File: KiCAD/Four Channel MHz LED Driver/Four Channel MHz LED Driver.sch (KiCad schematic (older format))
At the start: 89 parts, among them J1 Barrel_Jack_Switch, J10 Conn_01x08_Female, J2 Conn_01x02_Female, J3 8P8C_Shielded_x4, J4 Conn_01x05_Female, J5 Conn_01x24_Female, J6 Conn_01x03_Male, J7 Conn_01x24_Female, J8 Conn_01x03_Female, J9 Conn_01x03_Female, M1 Fan_4pin, Q2 SUM70060E, SW1 SW_SPDT, SW2 Pushbutton_with_LED_-_ELUMOAT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, SW3 Pushbutton_with_LED_-_ELUMOAT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, SW4 Pushbutton_with_LED_-_ELUMOAT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, SW5 Pushbutton_with_LED_-_ELUMOAT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, U1 12V boost, U10 LT6200CS8-10, U14 Teensy3.6, U16 SN74LV4T125PWR, U2 ASSR-1218, U3 DPBW06F-05, U4 BDJ0GA5WEFJ-E2, U5 ADP7182AUJZ-1.8-R7, U6 TMUX1204DGSR, U7 ASSR-1218, U8 ASSR-1218, U9 ASSR-1218

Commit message: Organized schematic
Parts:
- SW2, SW3, SW4, SW5: value Pushbutton_with_LED_-_ELUMOATHQ3C12 -> Pushbutton_with_LED
- renumbered C14 to C10, C15 to C11, C17 to C12, C34 to C13, C16 to C14, C9 to C15, C37 to C16, C19 to C17, C20 to C18, C12 to C19, C13 to C20, C23 to C21, C5 to C4, C6 to C5, C7 to C6, C10 to C7, C4 to C9, D4 to D3, D11 to D4, R5 to R1, R1 to R2, R2 to R5
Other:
- note added: "3.3V clamp for external analog\nMax voltage: +6V/-3V"
- note added: "4-pin 92mm fan"
- note added: "4x momentary pushbuttons with indicator LEDs"
- note added: "Constant Current LED Driver with Compensation\n\n"
- note added: "External analog input with 3.3V zener clamp"
- note added: "External thermistor and 3x 5V/16mA digital outputs\n"
- note added: "Inputs and Outputs\n"
- note added: "LED Solid-State Relay Mux\n\n"
- note added: "LED bypass capacitor array"
- note added: "Op-amp linear reagulator split supply: \n12V/-5V to clean 10V/-1.8V"
- note added: "Teensy 3.6 180 MHz Microcontroller"
- note added: "Thermal Management\n"
- note added: "Voltage Rails: 12V, 10V, 5V, -0.25V, -1.8V, -5V\n\n"
- note removed: "4-channel op-amp constant current LED driver"
- note removed: "External analog inputs with 5.6V zener clamp"
- note removed: "External thermistor and 3x 5V/16mA digital outputs\nOpen jumper for DAC output instead"
- note removed: "LDO: 12V to clean 5V for analog circuits"
- note removed: "LED bypass capacitors and connectors\nFor high current supplies use an in-line\ncapacitor with the power supply such as:\nUnited Chemi-Con E32D500HPN104MDA5M"
- note removed: "Op-amp split supply: 12V/-5V to clean 10V/-1.8V"
- moved on the sheet: BZ1, C1, C10, C11, C12, C13, C14, C17, C18, C19, C2, C20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

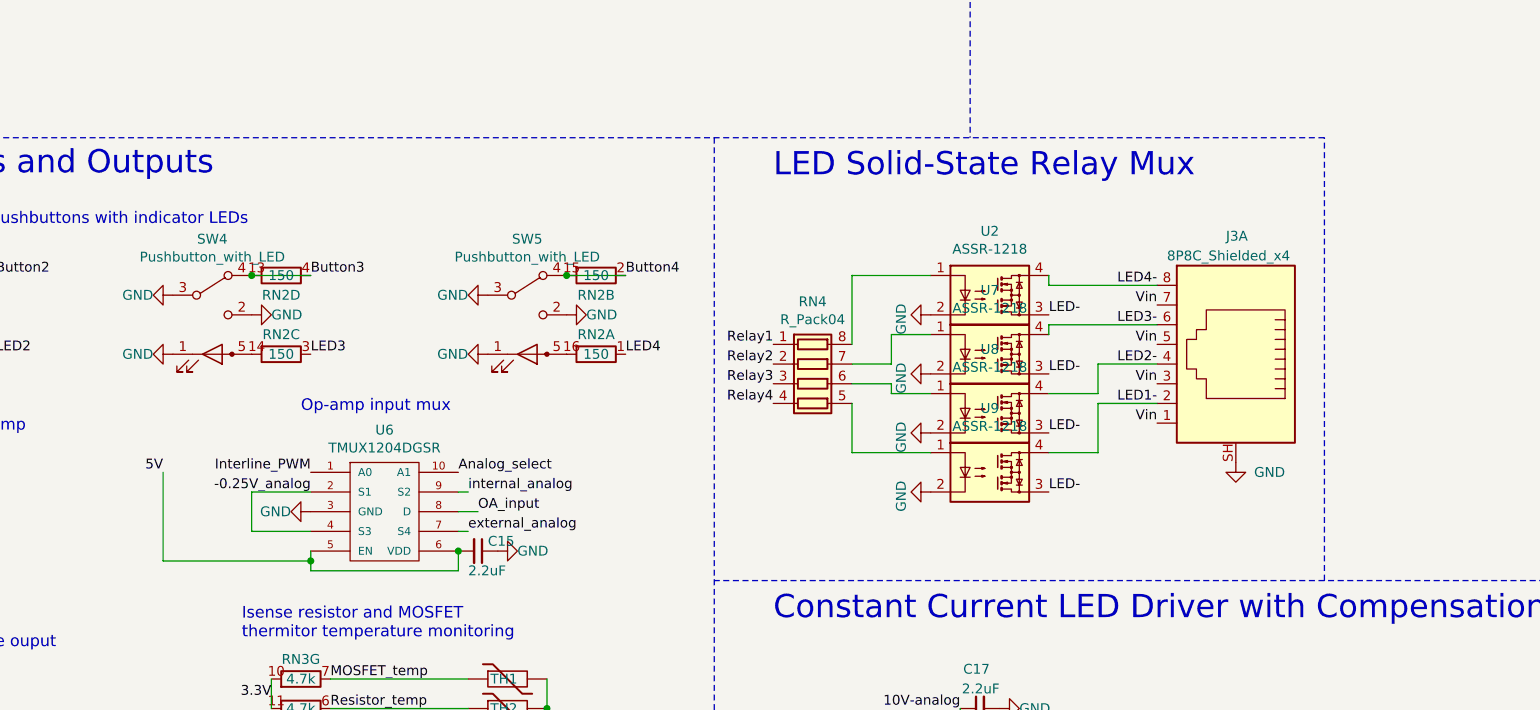
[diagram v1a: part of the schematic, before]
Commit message: Fix PCB after cleaned up schematic
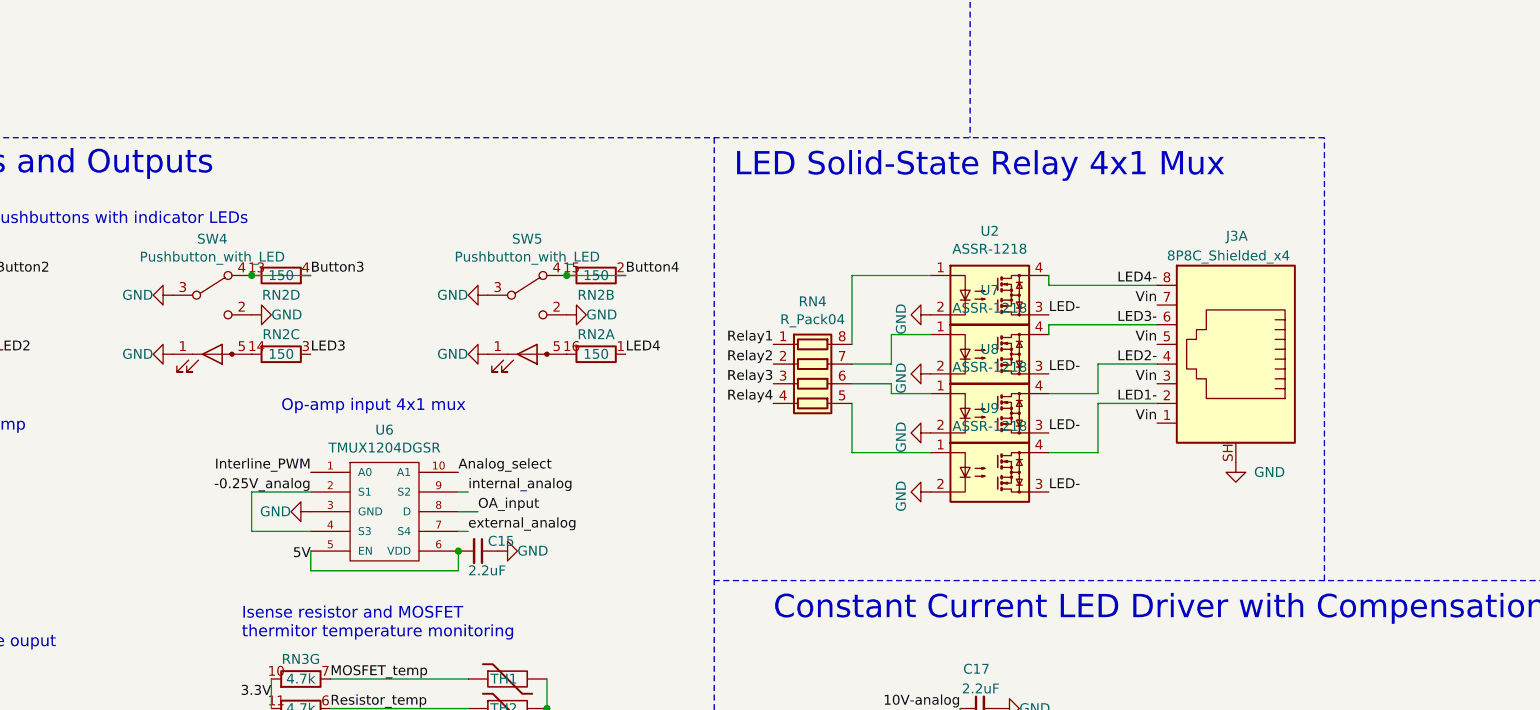
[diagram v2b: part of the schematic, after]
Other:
- note added: "LED Solid-State Relay 4x1 Mux\n\n"
- note added: "Op-amp input 4x1 mux"
- note removed: "LED Solid-State Relay Mux\n\n"
- note removed: "Op-amp input mux"
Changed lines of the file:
@@
 	0    1    1    0
 $EndComp
-Wire Wire Line
-	4650 6900 3900 6900
 $Comp
 L power:GND #PWR017
@@
 $EndComp
 Wire Wire Line
-	3900 6450 3900 6900
-Wire Wire Line
 	1600 6650 1850 6650
-Wire Wire Line
-	4650 6900 4650 6950
-Connection ~ 4650 6900
 $Comp
 L power:GND #PWR0148
@@
 Text Notes 850  8950 1    59   ~ 0
 I/O maximum voltage: +30V/-27V (160mW)\nNiDaq PCI-6110 is +/- 10V 5mA\n∴ minimum impedance is 2000 Ohms
-Text Notes 4600 6150 0    59   ~ 0
-Op-amp input mux
+Text Notes 4500 6150 0    59   ~ 0
+Op-amp input 4x1 mux
 Text Notes 2200 7350 0    59   ~ 0
 Current sense voltage ouput
@@
 Text Label 2150 6850 0    50   ~ 0
 external_analog
-Text Label 3900 6450 2    50   ~ 0
+Text Label 4650 6900 2    50   ~ 0
 5V
 Text Label 4650 6550 2    50   ~ 0
@@
 Wire Wire Line
 	4650 6950 5400 6950
-Wire Wire Line
-	4650 6850 4650 6900
 $Comp
 L Custom_parts:TMUX1204DGSR U6
@@
 Wire Notes Line
 	11800 7000 6700 7000
-Text Notes 7000 5150 0    118  ~ 0
-LED Solid-State Relay Mux\n\n
+Text Notes 6800 5150 0    118  ~ 0
+LED Solid-State Relay 4x1 Mux\n\n
 Text Notes 10850 750  0    118  ~ 0
 Teensy 3.6 180 MHz Microcontroller
@@
 Wire Notes Line
 	8000 500  8000 4750
+Wire Wire Line
+	4650 6850 4650 6950
 $EndSCHEMATC

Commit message: Re-annotate DRC pass
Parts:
- renumbered C7 to C1, C9 to C10, C19 to C11, C20 to C12, C10 to C13, C11 to C14, C14 to C15, C15 to C16, C12 to C17, C13 to C18, C17 to C19, C1 to C2, C18 to C20, C2 to C3, C3 to C4, C4 to C5, C5 to C6, C6 to C7, C16 to C9, D5 to D4, D4 to D5, H2 to H1, H3 to H2, H1 to H3, H14 to H5, H15 to H6, H16 to H7, H17 to H8, J7 to J10, J6 to J4, J9 to J5, J10 to J6, J8 to J7, J4 to J8, J5 to J9, JP4 to JP2, JP2 to JP3, JP5 to JP4, JP3 to JP5, Q2 to Q1, R5 to R1, R6 to R2, R1 to R3, R2 to R4, R3 to R5, R4 to R6, RN2 to RN1, RN1 to RN2, RV3 to RV1, RV1 to RV2, RV2 to RV3, SW2 to SW1, SW3 to SW2, SW4 to SW3, SW1 to SW4, U8 to U10, U9 to U11, U14 to U12, U16 to U2, U6 to U4, U4 to U5, U5 to U6, U10 to U7, U2 to U8, U7 to U9

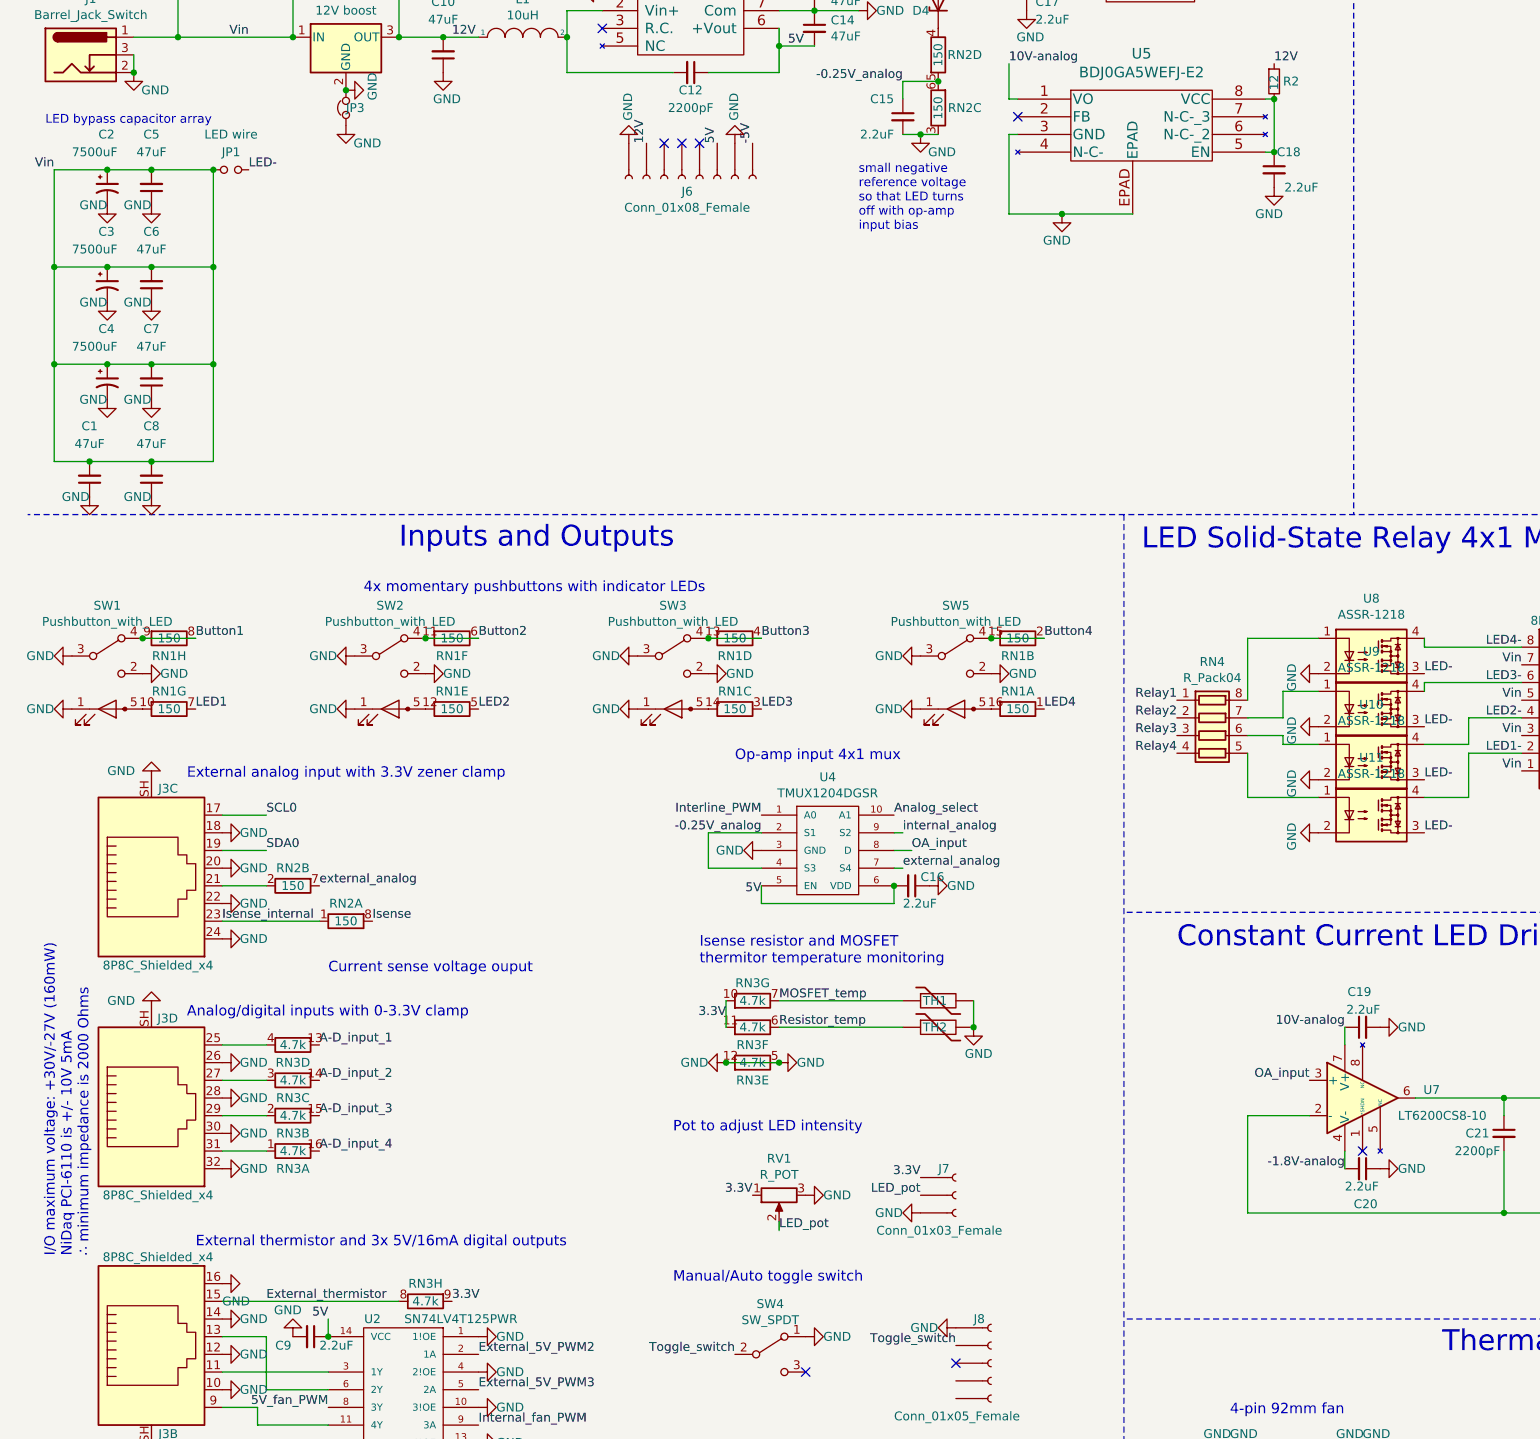
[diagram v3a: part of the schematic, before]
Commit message: Fix footprints and position silkscreen labels
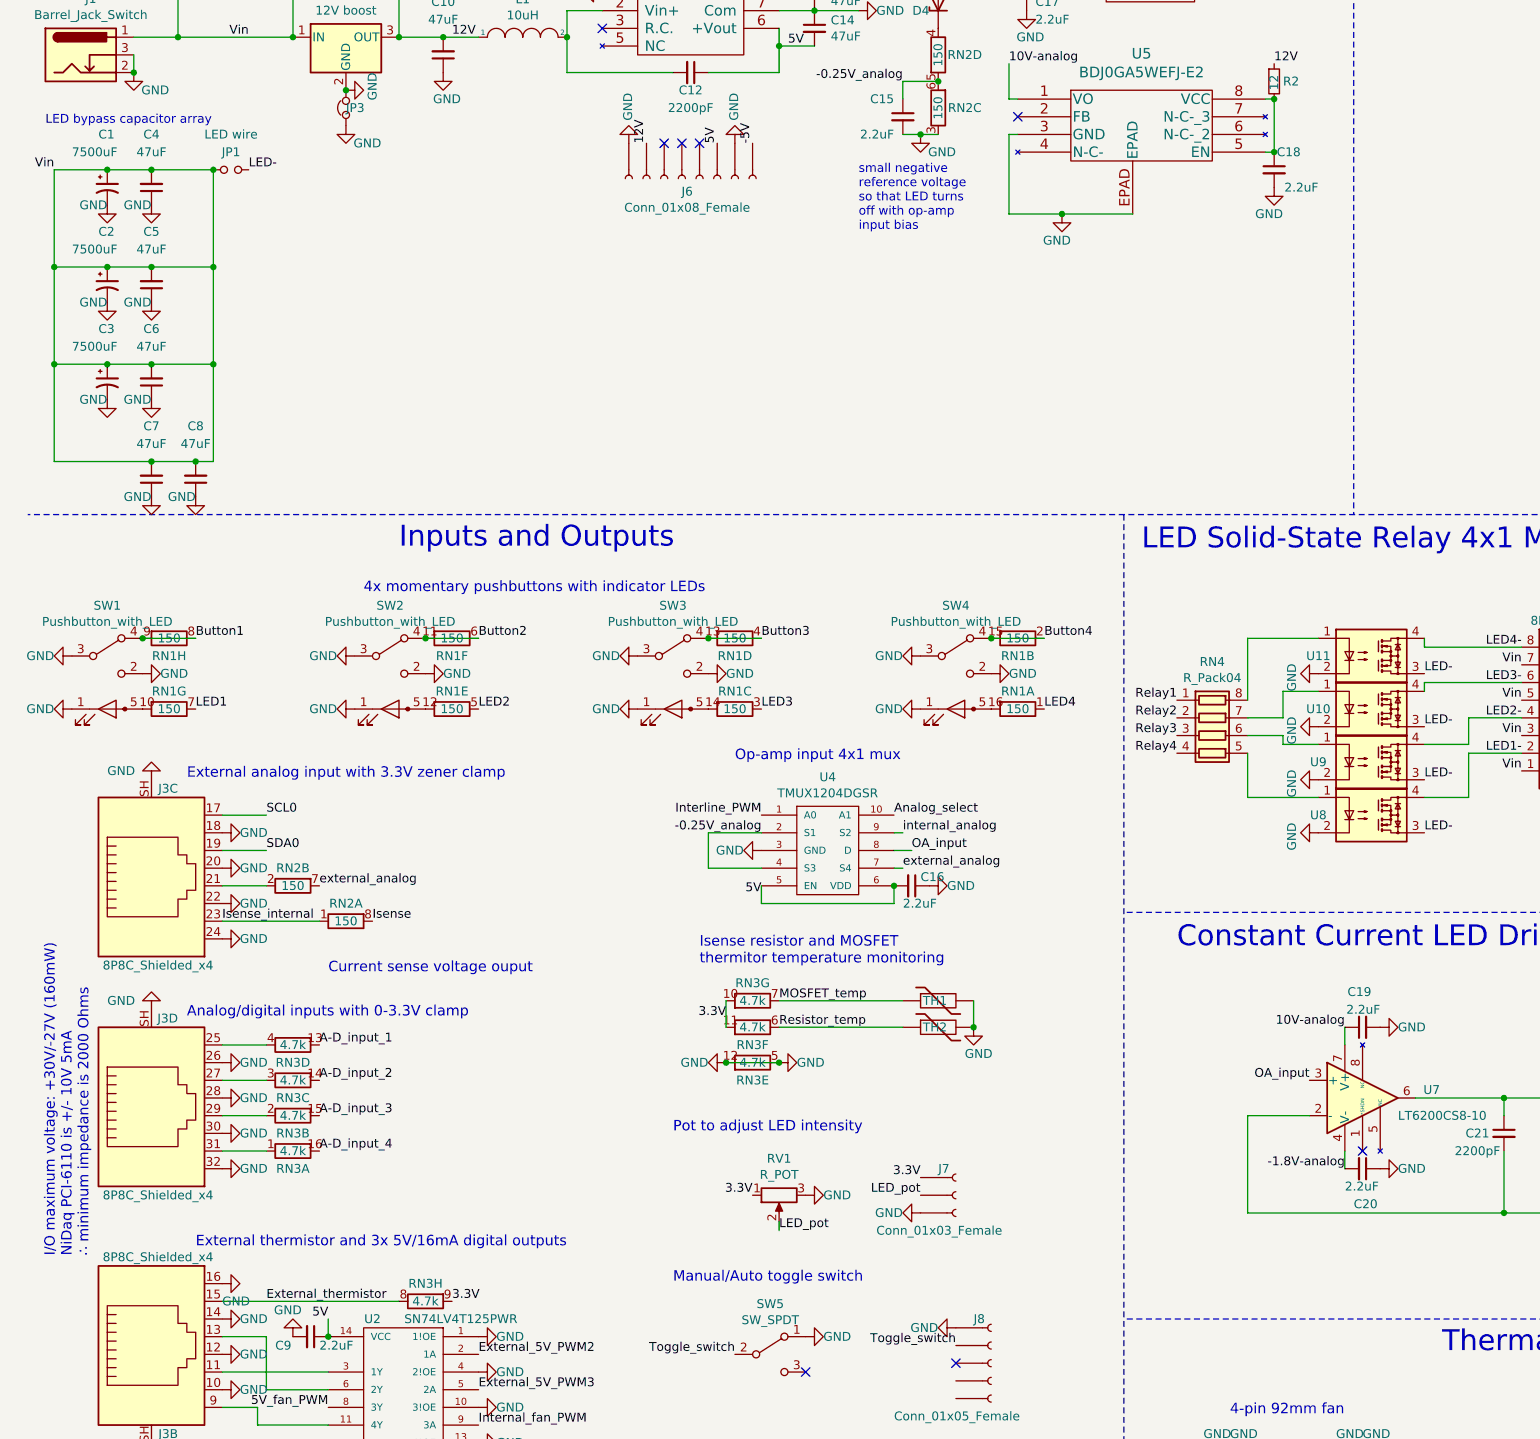
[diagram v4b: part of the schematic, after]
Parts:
- renumbered C3 to C1, C4 to C3, C5 to C4, C6 to C5, C7 to C6, C8 to C7, C1 to C8, R5 to R3, R6 to R4, R3 to R5, R4 to R6, SW5 to SW4, SW4 to SW5, U9 to U10, U8 to U11, U11 to U8, U10 to U9
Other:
- moved on the sheet: C1, C2, C8, R3, R4, R5, R6

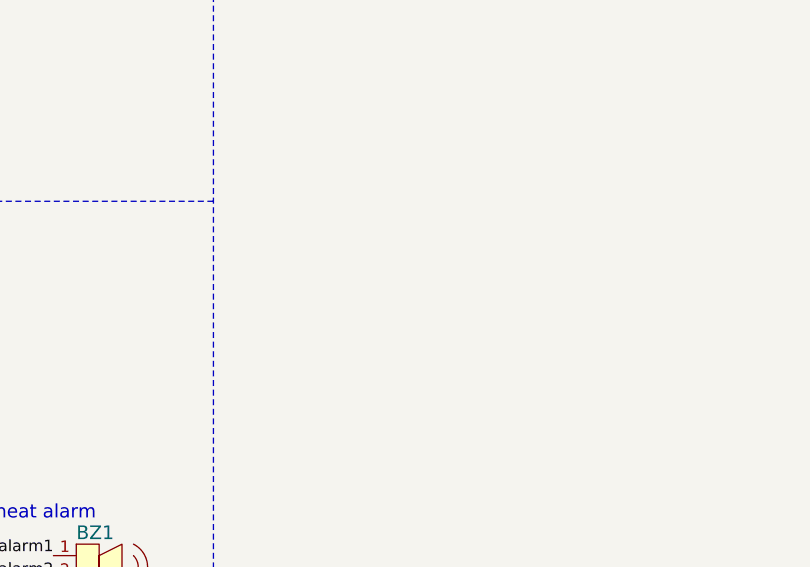
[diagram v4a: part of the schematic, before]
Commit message: Add logos to schematic and PCB
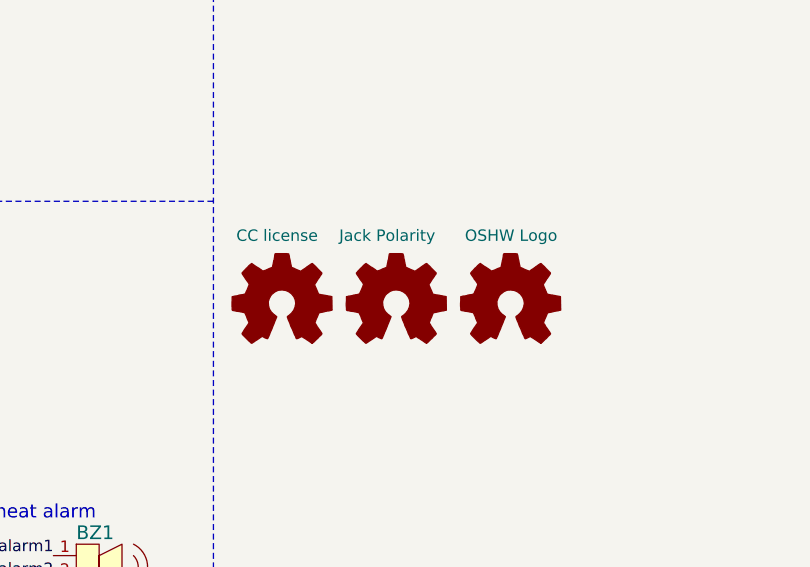
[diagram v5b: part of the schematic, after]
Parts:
- added LOGO1: CC license, Custom Footprints:Creative_commons_license, symbol Graphic:Logo_Open_Hardware_Small
- added LOGO2: Jack Polarity, Custom Footprints:Polarity_Center_Positive, symbol Graphic:Logo_Open_Hardware_Small
- added LOGO3: OSHW Logo, Symbol:OSHW-Logo2_7.3x6mm_SilkScreen, symbol Graphic:Logo_Open_Hardware_Small
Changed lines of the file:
@@
 Wire Wire Line
 	650  4450 1200 4450
+$Comp
+L Graphic:Logo_Open_Hardware_Small LOGO1
+U 1 1 5FF69CC3
+P 12100 9750
+F 0 "LOGO1" H 12100 10025 50  0001 C CNN
+F 1 "CC license" H 11900 10050 50  0000 L CNN
+F 2 "Custom Footprints:Creative_commons_license" H 12100 9750 50  0001 C CNN
+F 3 "~" H 12100 9750 50  0001 C CNN
+	1    12100 9750
+	1    0    0    -1
+$EndComp
+$Comp
+L Graphic:Logo_Open_Hardware_Small LOGO2
+U 1 1 5FF6ADDD
+P 12600 9750
+F 0 "LOGO2" H 12600 10025 50  0001 C CNN
+F 1 "Jack Polarity" H 12350 10050 50  0000 L CNN
+F 2 "Custom Footprints:Polarity_Center_Positive" H 12600 9750 50  0001 C CNN
+F 3 "~" H 12600 9750 50  0001 C CNN
+	1    12600 9750
+	1    0    0    -1
+$EndComp
+$Comp
+L Graphic:Logo_Open_Hardware_Small LOGO3
+U 1 1 5FF6B1EE
+P 13100 9750
+F 0 "LOGO3" H 13100 10025 50  0001 C CNN
+F 1 "OSHW Logo" H 12900 10050 50  0000 L CNN
+F 2 "Symbol:OSHW-Logo2_7.3x6mm_SilkScreen" H 13100 9750 50  0001 C CNN
+F 3 "~" H 13100 9750 50  0001 C CNN
+	1    13100 9750
+	1    0    0    -1
+$EndComp
 $EndSCHEMATC

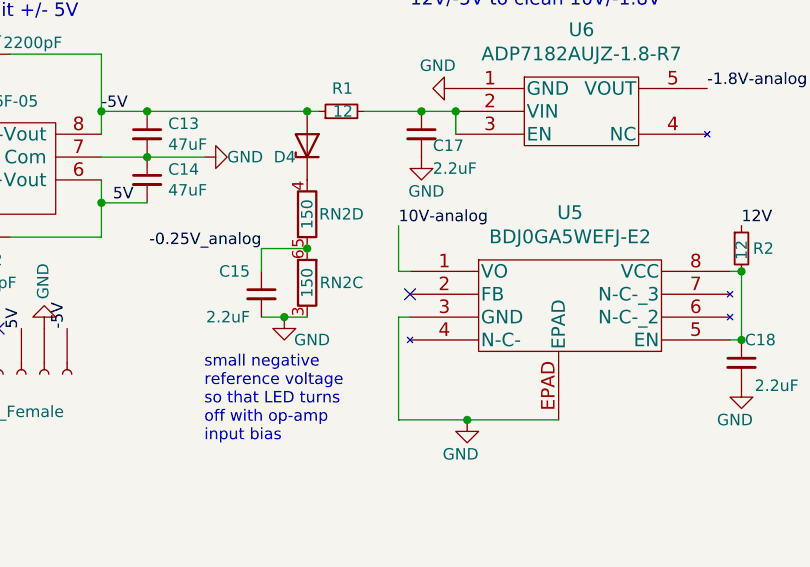
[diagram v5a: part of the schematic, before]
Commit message: Fixed error of disconnected FB pin on 10V LDO and improved cap placement
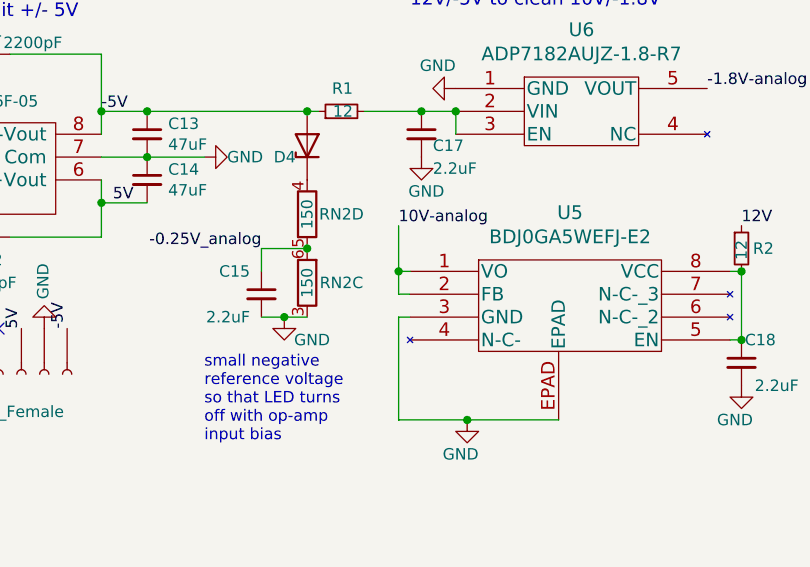
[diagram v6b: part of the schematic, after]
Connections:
- net 10V-analog: now also U5.2 (FB)
- no-connect marks 52 -> 51
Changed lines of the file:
@@
 Wire Wire Line
 	6100 2400 6050 2400
-NoConn ~ 6100 2500
 Wire Wire Line
 	6750 3050 6350 3050
@@
 	1    0    0    -1
 $EndComp
+Wire Wire Line
+	6050 2400 6050 2500
+Wire Wire Line
+	6050 2500 6100 2500
+Connection ~ 6050 2400
 $EndSCHEMATC
